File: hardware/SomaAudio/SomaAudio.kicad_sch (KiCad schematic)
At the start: 14 parts, among them CN1 0.1uF, CN2 0.1uF, IC1 DG406DJ, J17 I2C, J2 Audio GND +, J3 Audio Out, J4 VIN, J5 Audio IN 1, J6 Audio IN 2, U1 MCP23017_SP

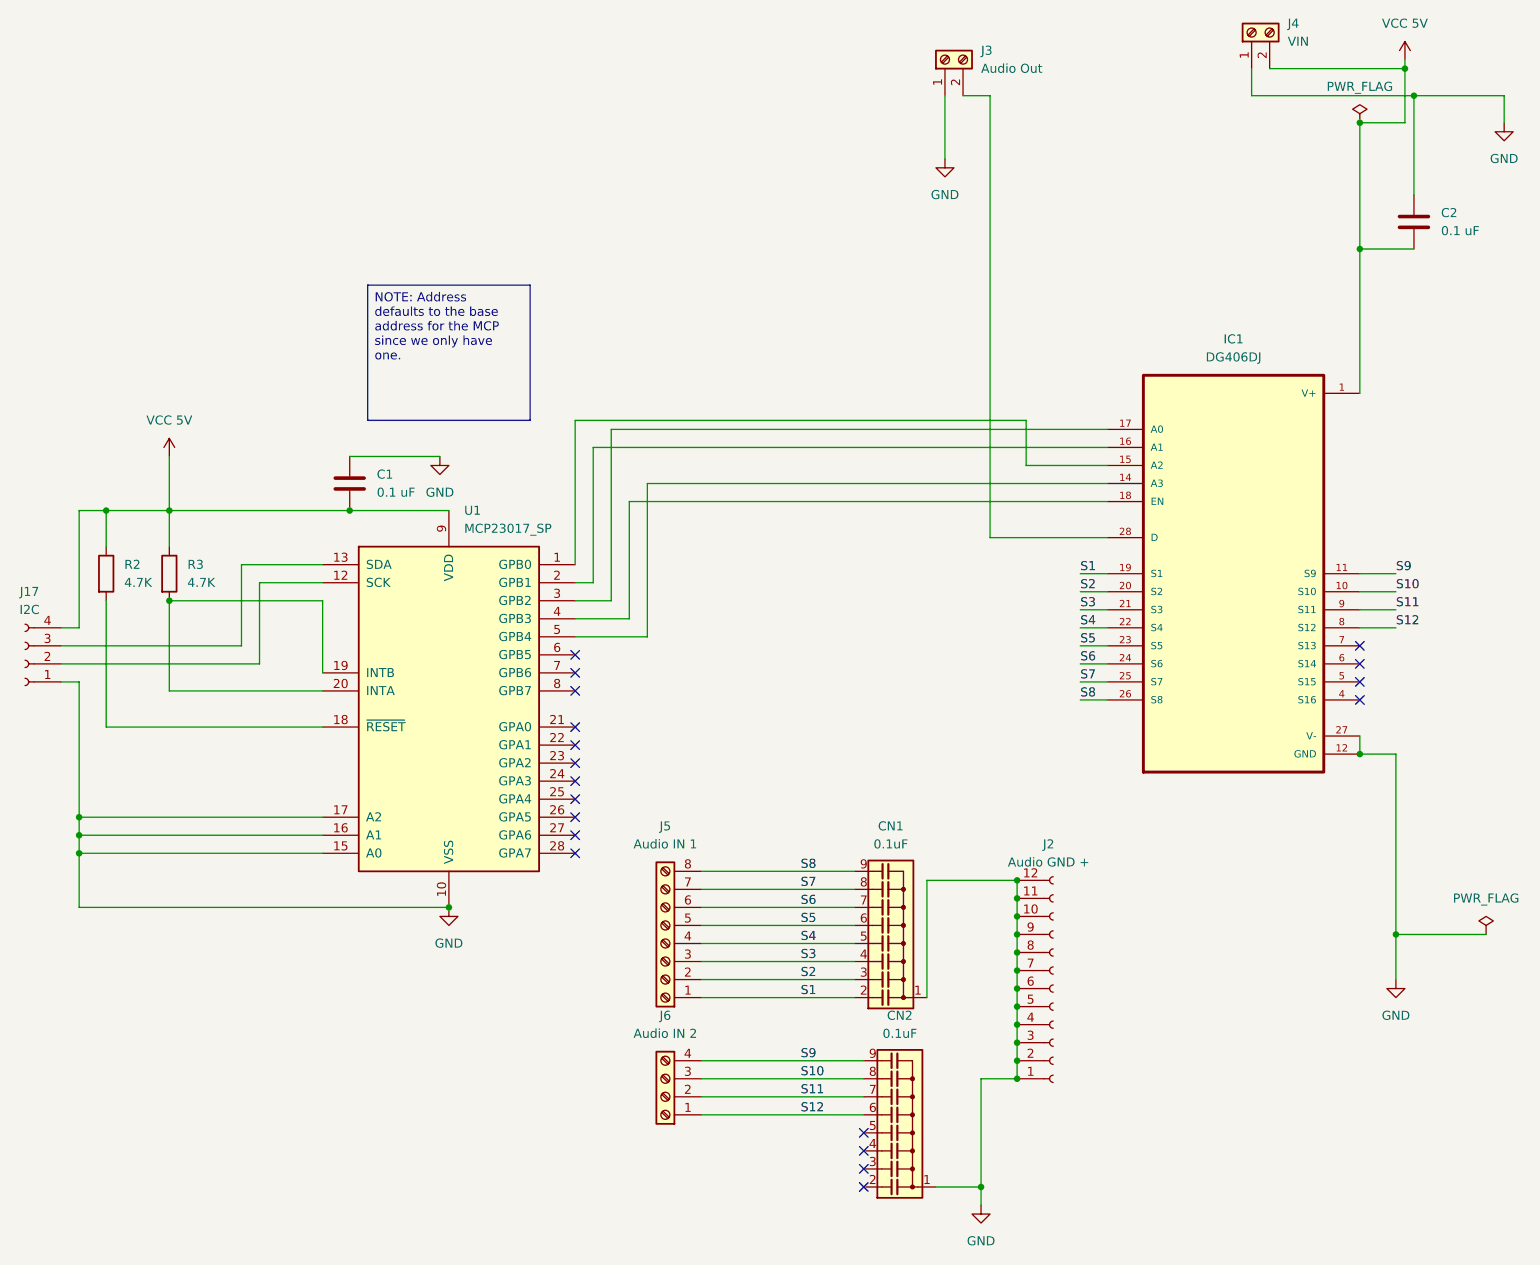
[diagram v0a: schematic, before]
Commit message: hardware: combo board, LED board, production outputs, arduino firmware
Co-Authored-By: Claude Opus 5.5 (1M context) <noreply@anthropic.com>
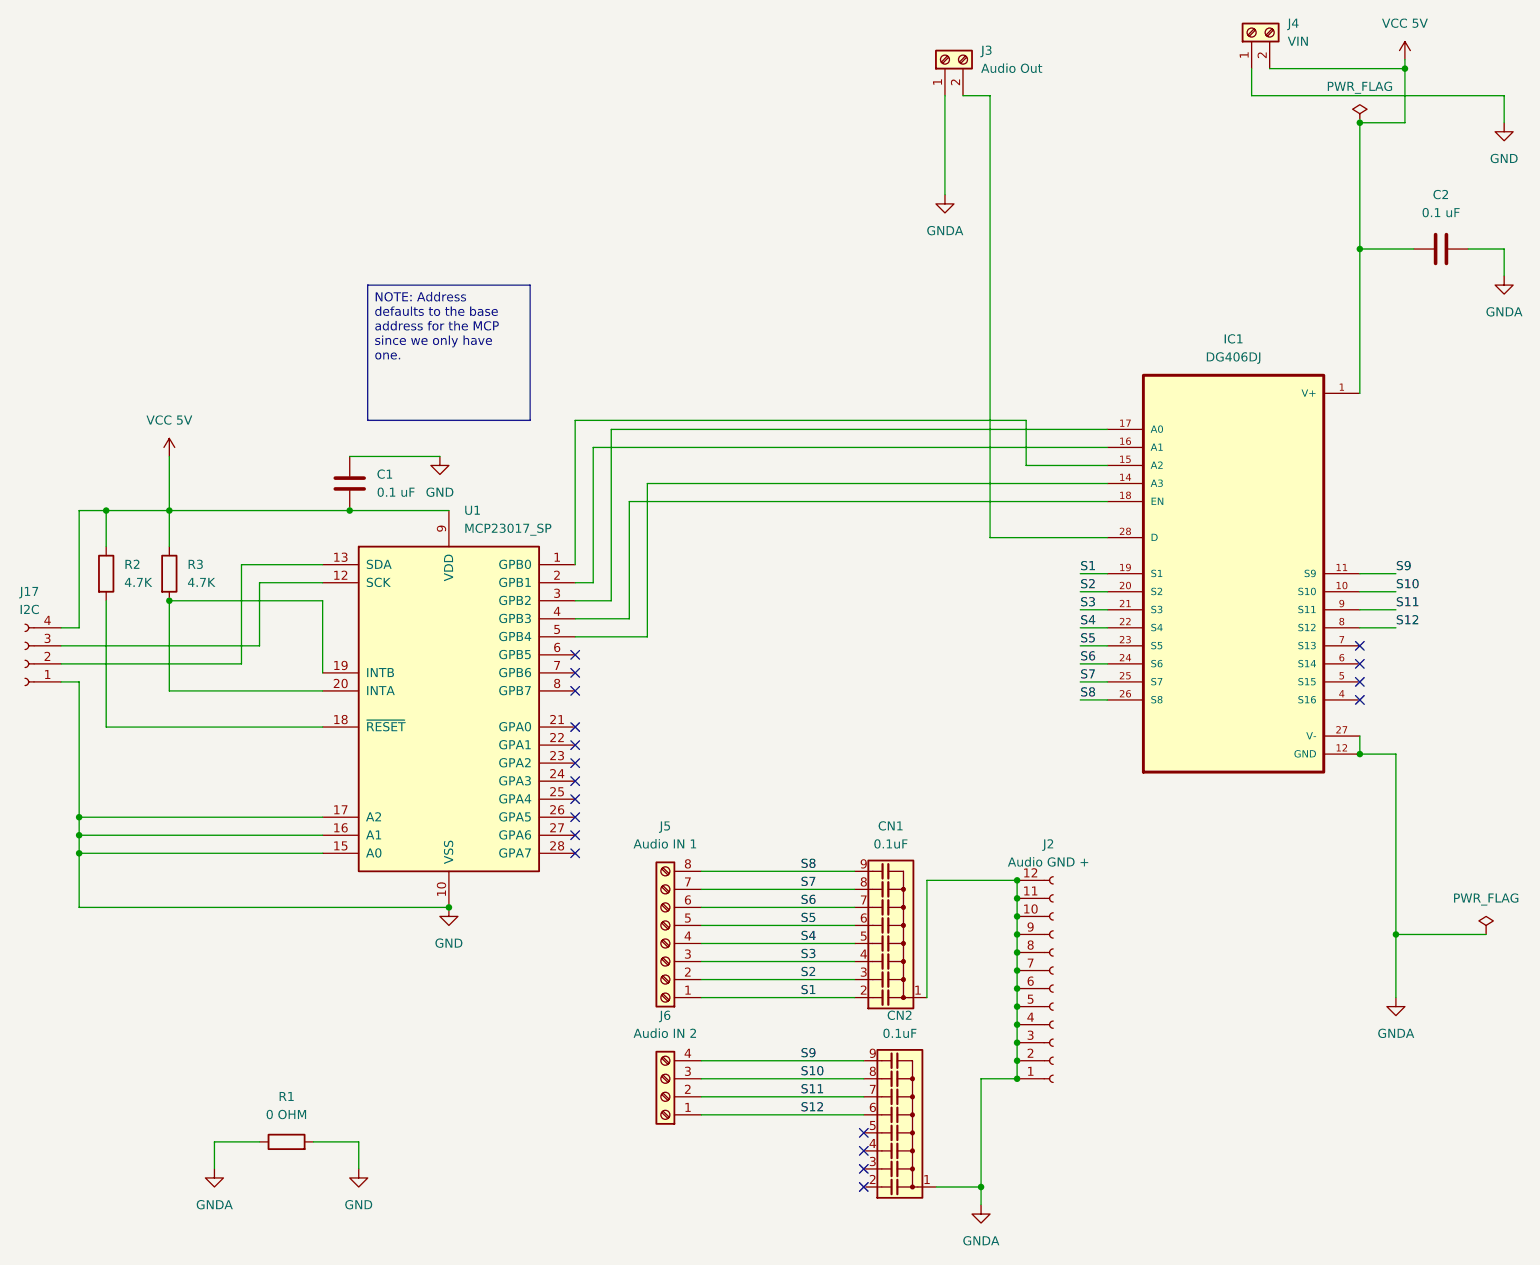
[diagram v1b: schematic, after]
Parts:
- added R1: 0 OHM, Resistor_THT:R_Axial_DIN0204_L3.6mm_D1.6mm_P5.08mm_Horizontal, symbol Device:R
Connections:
- net GND: now also R1.2; no longer C2.1, CN1.1 (common), CN2.1 (common), IC1.12 (GND), IC1.27 (V-), J2.1 (Pin_1), J2.10 (Pin_10), J2.11 (Pin_11), J2.12 (Pin_12), J2.2 (Pin_2), J2.3 (Pin_3), J2.4 (Pin_4), J2.5 (Pin_5), J2.6 (Pin_6), J2.7 (Pin_7), J2.8 (Pin_8), J2.9 (Pin_9), J3.1 (Pin_1)
- net VCC 5V: now also C2.1; no longer C2.2
- net at J17.2 (Pin_2): now also U1.13 (SDA); no longer U1.12 (SCK)
- net at J17.3 (Pin_3): now also U1.12 (SCK); no longer U1.13 (SDA)
- new net GNDA: C2.2, CN1.1 (common), CN2.1 (common), IC1.12 (GND), IC1.27 (V-), J2.1 (Pin_1), J2.10 (Pin_10), J2.11 (Pin_11), J2.12 (Pin_12), J2.2 (Pin_2), J2.3 (Pin_3), J2.4 (Pin_4), J2.5 (Pin_5), J2.6 (Pin_6), J2.7 (Pin_7), J2.8 (Pin_8), J2.9 (Pin_9), J3.1 (Pin_1), R1.1
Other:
- moved on the sheet: C2
